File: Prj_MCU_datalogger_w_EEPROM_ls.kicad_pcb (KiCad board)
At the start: 2 copper layers, 57.1 x 36.8 mm, 29 parts, among them J1 Conn_01x04_Pin, J2 Conn_01x04_Pin, J3 Conn_01x09_Pin, J4 Conn_02x03_Odd_Even, U1 24LC1025, U2 24LC1025, U3 ATMEGA328P-AU, U4 DS1337S_, Y1 16 MHz, Y2 32.768 kHz

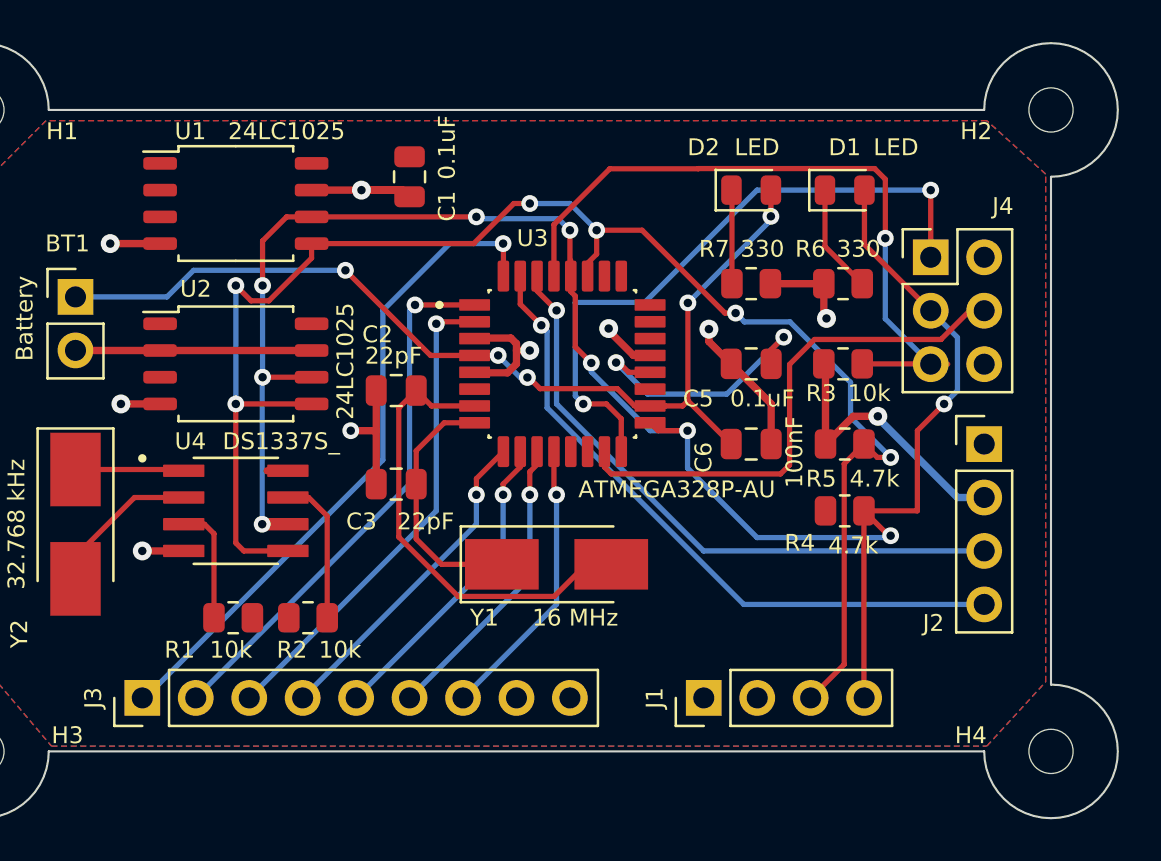
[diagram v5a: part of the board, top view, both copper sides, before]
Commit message: Refined routing.v3
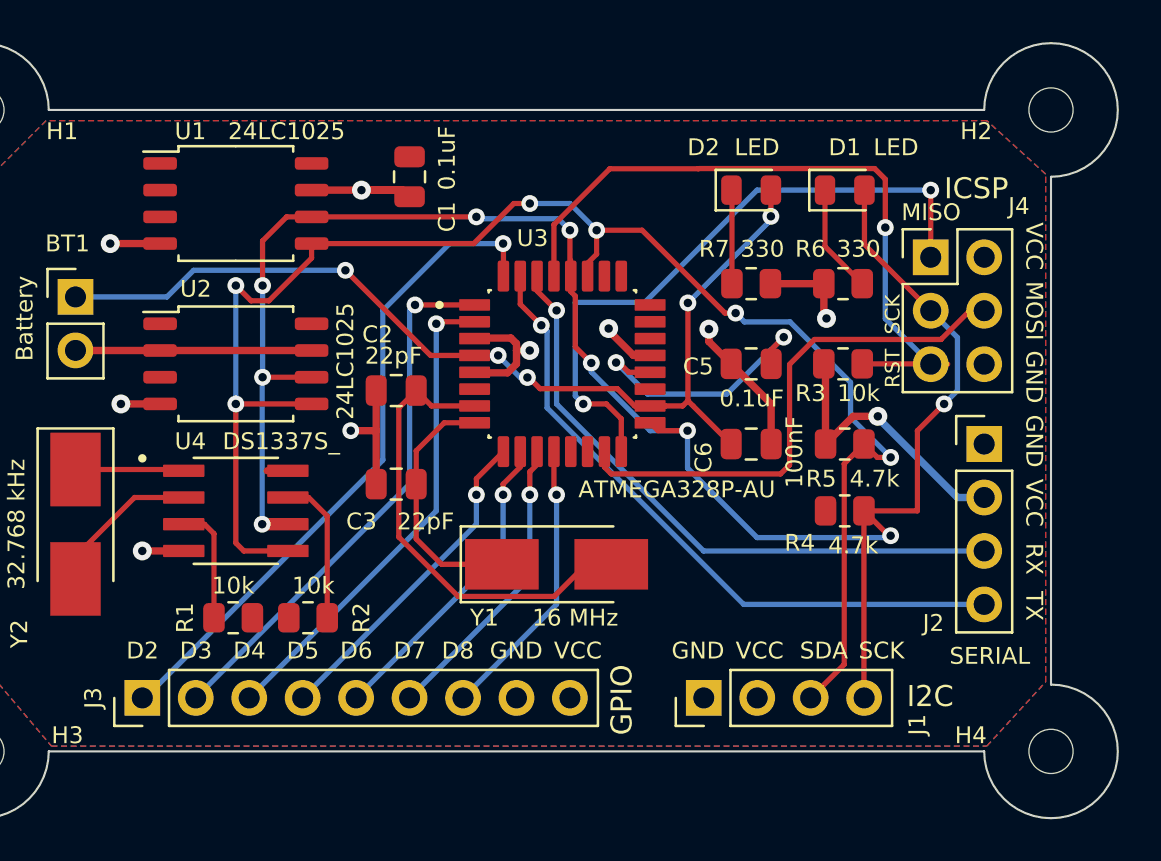
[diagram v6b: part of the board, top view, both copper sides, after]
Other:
- board text added: "D2"
- board text added: "D3"
- board text added: "D4"
- board text added: "D5"
- board text added: "D6"
- board text added: "D7"
- board text added: "D8"
- board text added: "GND"
- board text added: "GPIO"
- board text added: "I2C"
- board text added: "ICSP"
- board text added: "MISO"
- board text added: "MOSI"
- board text added: "RST"
- board text added: "RX"
- board text added: "SCK"
- board text added: "SDA"
- board text added: "SERIAL"
- board text added: "TX"
- board text added: "VCC"
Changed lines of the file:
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@@
     (property "ki_keywords" "connector")
     (attr through_hole)
-    (fp_text reference "J1" (at 0 -2.33 90) (layer "F.SilkS")
+    (fp_text reference "J1" (at -1.27 10.15 90) (layer "F.SilkS")
         (effects (font (size 0.8 0.8) (thickness 0.15)))
     )
@@
     (property "ki_keywords" "cap capacitor")
     (attr smd)
-    (fp_text reference "C5" (at -2.5165 1.651 180) (layer "F.SilkS")
-        (effects (font (size 0.8 0.8) (thickness 0.15)))
-    )
-    (fp_text value "0.1uF" (at 0.5315 1.651) (layer "F.SilkS")
+    (fp_text reference "C5" (at -2.5165 0.127 180) (layer "F.SilkS")
+        (effects (font (size 0.8 0.8) (thickness 0.15)))
+    )
+    (fp_text value "0.1uF" (at 0.0235 1.651) (layer "F.SilkS")
         (effects (font (size 0.8 0.8) (thickness 0.15)))
     )
@@
     (property "ki_keywords" "cap capacitor")
     (attr smd)
-    (fp_text reference "C1" (at 1.397 -1.778 90) (layer "F.SilkS")
-        (effects (font (size 0.8 0.8) (thickness 0.15)))
-    )
-    (fp_text value "0.1uF" (at -1.397 -1.778 90) (layer "F.SilkS")
+    (fp_text reference "C1" (at 1.905 -1.778 90) (layer "F.SilkS")
+        (effects (font (size 0.8 0.8) (thickness 0.15)))
+    )
+    (fp_text value "0.1uF" (at -0.889 -1.778 90) (layer "F.SilkS")
         (effects (font (size 0.8 0.8) (thickness 0.15)))
     )
@@
     (property "ki_keywords" "R res resistor")
     (attr smd)
-    (fp_text reference "R2" (at -0.762 1.524) (layer "F.SilkS")
-        (effects (font (size 0.8 0.8) (thickness 0.15)))
-    )
-    (fp_text value "10k" (at 1.524 1.524) (layer "F.SilkS")
+    (fp_text reference "R2" (at 2.54 0 90) (layer "F.SilkS")
+        (effects (font (size 0.8 0.8) (thickness 0.15)))
+    )
+    (fp_text value "10k" (at 0.254 -1.524) (layer "F.SilkS")
         (effects (font (size 0.8 0.8) (thickness 0.15)))
     )
@@
     (property "ki_keywords" "R res resistor")
     (attr smd)
-    (fp_text reference "R3" (at -1.0395 1.397) (layer "F.SilkS")
-        (effects (font (size 0.8 0.8) (thickness 0.15)))
-    )
-    (fp_text value "10k" (at 1.2465 1.397) (layer "F.SilkS")
+    (fp_text reference "R3" (at -1.5475 1.397) (layer "F.SilkS")
+        (effects (font (size 0.8 0.8) (thickness 0.15)))
+    )
+    (fp_text value "10k" (at 0.7385 1.397) (layer "F.SilkS")
         (effects (font (size 0.8 0.8) (thickness 0.15)))
     )
@@
     (property "ki_keywords" "connector")
     (attr through_hole)
-    (fp_text reference "J4" (at 3.429 -2.428) (layer "F.SilkS")
+    (fp_text reference "J4" (at 4.191 -2.428) (layer "F.SilkS")
         (effects (font (size 0.8 0.8) (thickness 0.15)))
     )
@@
     (property "ki_keywords" "R res resistor")
     (attr smd)
-    (fp_text reference "R1" (at 2.54 -1.524) (layer "F.SilkS")
-        (effects (font (size 0.8 0.8) (thickness 0.15)))
-    )
-    (fp_text value "10k" (at 0.1035 -1.524) (layer "F.SilkS")
+    (fp_text reference "R1" (at 2.286 0 90) (layer "F.SilkS")
+        (effects (font (size 0.8 0.8) (thickness 0.15)))
+    )
+    (fp_text value "10k" (at 0 1.524) (layer "F.SilkS")
         (effects (font (size 0.8 0.8) (thickness 0.15)))
     )
@@
   (gr_arc (start 271.78 154.305) (mid 274.025064 159.725064) (end 268.605 157.48)
     (stroke (width 0.1) (type default)) (layer "Edge.Cuts"))
+  (gr_text "GND" (at 270.51 138.43 270) (layer "F.SilkS")
+    (effects (font (size 0.8 0.8) (thickness 0.15)) (justify left bottom))
+  )
+  (gr_text "TX" (at 270.51 149.86 270) (layer "F.SilkS")
+    (effects (font (size 0.8 0.8) (thickness 0.15)) (justify left bottom))
+  )
+  (gr_text "D8" (at 242.824 153.162) (layer "F.SilkS")
+    (effects (font (size 0.8 0.8) (thickness 0.15)) (justify left bottom))
+  )
+  (gr_text "D2" (at 227.838 153.162) (layer "F.SilkS")
+    (effects (font (size 0.8 0.8) (thickness 0.15)) (justify left bottom))
+  )
+  (gr_text "D7" (at 240.538 153.162) (layer "F.SilkS")
+    (effects (font (size 0.8 0.8) (thickness 0.15)) (justify left bottom))
+  )
+  (gr_text "GND" (at 245.11 153.162) (layer "F.SilkS")
+    (effects (font (size 0.8 0.8) (thickness 0.15)) (justify left bottom))
+  )
+  (gr_text "SCK" (at 264.668 137.668 90) (layer "F.SilkS")
+    (effects (font (size 0.7 0.7) (thickness 0.15)) (justify left bottom))
+  )
+  (gr_text "D4" (at 232.918 153.162) (layer "F.SilkS")
+    (effects (font (size 0.8 0.8) (thickness 0.15)) (justify left bottom))
+  )
+  (gr_text "VCC" (at 270.51 132.334 270) (layer "F.SilkS")
+    (effects (font (size 0.8 0.8) (thickness 0.15)) (justify left bottom))
+  )
+  (gr_text "MISO" (at 264.668 132.334) (layer "F.SilkS")
+    (effects (font (size 0.8 0.8) (thickness 0.15)) (justify left bottom))
+  )
+  (gr_text "MOSI" (at 270.51 135.128 270) (layer "F.SilkS")
+    (effects (font (size 0.8 0.8) (thickness 0.15)) (justify left bottom))
+  )
+  (gr_text "VCC" (at 270.51 144.526 -90) (layer "F.SilkS")
+    (effects (font (size 0.8 0.8) (thickness 0.15)) (justify left bottom))
+  )
+  (gr_text "SERIAL" (at 266.954 153.416) (layer "F.SilkS")
+    (effects (font (size 0.8 0.8) (thickness 0.15)) (justify left bottom))
+  )
+  (gr_text "VCC" (at 256.794 153.162) (layer "F.SilkS")
+    (effects (font (size 0.8 0.8) (thickness 0.15)) (justify left bottom))
+  )
+  (gr_text "I2C" (at 264.922 155.448) (layer "F.SilkS")
+    (effects (font (size 1 1) (thickness 0.15)) (justify left bottom))
+  )
+  (gr_text "D5" (at 235.458 153.162) (layer "F.SilkS")
+    (effects (font (size 0.8 0.8) (thickness 0.15)) (justify left bottom))
+  )
+  (gr_text "ICSP" (at 266.7 131.318) (layer "F.SilkS")
+    (effects (font (size 1 1) (thickness 0.15)) (justify left bottom))
+  )
+  (gr_text "SDA" (at 259.842 153.162) (layer "F.SilkS")
+    (effects (font (size 0.8 0.8) (thickness 0.15)) (justify left bottom))
+  )
+  (gr_text "RST" (at 264.668 140.208 90) (layer "F.SilkS")
+    (effects (font (size 0.7 0.7) (thickness 0.15)) (justify left bottom))
+  )
+  (gr_text "GPIO" (at 251.968 156.718 90) (layer "F.SilkS")
+    (effects (font (size 1 1) (thickness 0.15)) (justify left bottom))
+  )
+  (gr_text "D3" (at 230.378 153.162) (layer "F.SilkS")
+    (effects (font (size 0.8 0.8) (thickness 0.15)) (justify left bottom))
+  )
+  (gr_text "VCC" (at 248.158 153.162) (layer "F.SilkS")
+    (effects (font (size 0.8 0.8) (thickness 0.15)) (justify left bottom))
+  )
+  (gr_text "GND" (at 253.746 153.162) (layer "F.SilkS")
+    (effects (font (size 0.8 0.8) (thickness 0.15)) (justify left bottom))
+  )
+  (gr_text "SCK" (at 262.636 153.162) (layer "F.SilkS")
+    (effects (font (size 0.8 0.8) (thickness 0.15)) (justify left bottom))
+  )
+  (gr_text "D6" (at 237.998 153.162) (layer "F.SilkS")
+    (effects (font (size 0.8 0.8) (thickness 0.15)) (justify left bottom))
+  )
+  (gr_text "RX" (at 270.51 147.574 270) (layer "F.SilkS")
+    (effects (font (size 0.8 0.8) (thickness 0.15)) (justify left bottom))
+  )
+  (gr_text "GND" (at 270.51 141.478 -90) (layer "F.SilkS")
+    (effects (font (size 0.8 0.8) (thickness 0.15)) (justify left bottom))
+  )
   (segment (start 238.252 134.62) (end 242.297 138.665) (width 0.25) (layer "F.Cu") (net 1))
   (segment (start 251.175001 140.245) (end 251.995001 141.065) (width 0.25) (layer "F.Cu") (net 1))
@@
   (segment (start 267.916701 136.54) (end 266.551701 137.905) (width 0.25) (layer "F.Cu") (net 21))
   (segment (start 250.56 143.969999) (end 250.56 143.235) (width 0.25) (layer "F.Cu") (net 21))
+  (segment (start 263.906 130.289912) (end 263.401088 129.785) (width 0.25) (layer "F.Cu") (net 22))
+  (segment (start 248.16 132.449695) (end 248.16 134.895) (width 0.25) (layer "F.Cu") (net 22))
   (segment (start 266.872588 139.08) (end 266.065 139.08) (width 0.25) (layer "F.Cu") (net 22))
+  (segment (start 255.025 129.785) (end 255.016 129.794) (width 0.25) (layer "F.Cu") (net 22))
   (segment (start 266.05 139.065) (end 266.065 139.08) (width 0.25) (layer "F.Cu") (net 22))
-  (segment (start 263.401088 129.785) (end 263.906 130.289912) (width 0.25) (layer "F.Cu") (net 22))
+  (segment (start 263.906 132.588) (end 263.906 130.289912) (width 0.25) (layer "F.Cu") (net 22))
   (segment (start 262.81 139.065) (end 266.05 139.065) (width 0.25) (layer "F.Cu") (net 22))
-  (segment (start 255.025 129.785) (end 263.401088 129.785) (width 0.25) (layer "F.Cu") (net 22))
-  (segment (start 248.16 132.449695) (end 250.815695 129.794) (width 0.25) (layer "F.Cu") (net 22))
-  (segment (start 248.16 134.895) (end 248.16 132.449695) (width 0.25) (layer "F.Cu") (net 22))
-  (segment (start 255.016 129.794) (end 255.025 129.785) (width 0.25) (layer "F.Cu") (net 22))
-  (segment (start 250.815695 129.794) (end 255.016 129.794) (width 0.25) (layer "F.Cu") (net 22))
-  (segment (start 263.906 130.289912) (end 263.906 133.096) (width 0.25) (layer "F.Cu") (net 22))
-  (via (at 263.906 133.096) (size 0.8) (drill 0.4) (layers "F.Cu" "B.Cu") (net 22))
+  (segment (start 263.401088 129.785) (end 255.025 129.785) (width 0.25) (layer "F.Cu") (net 22))
+  (segment (start 255.016 129.794) (end 250.815695 129.794) (width 0.25) (layer "F.Cu") (net 22))
+  (segment (start 250.815695 129.794) (end 248.16 132.449695) (width 0.25) (layer "F.Cu") (net 22))
+  (via (at 263.906 132.588) (size 0.8) (drill 0.4) (layers "F.Cu" "B.Cu") (net 22))
+  (segment (start 263.906 132.588) (end 263.906 136.921) (width 0.25) (layer "B.Cu") (net 22))
   (segment (start 263.906 136.921) (end 266.065 139.08) (width 0.25) (layer "B.Cu") (net 22))
-  (segment (start 263.906 133.096) (end 263.906 136.921) (width 0.25) (layer "B.Cu") (net 22))
   (segment (start 231.554999 146.685) (end 230.57 146.685) (width 0.25) (layer "F.Cu") (net 23))
   (segment (start 232.0055 147.135501) (end 231.554999 146.685) (width 0.25) (layer "F.Cu") (net 23))

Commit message: Refined routing.v4
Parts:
- moved C2 0.38 mm to (240.7, 140.7)
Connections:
- BT1 pad 1: Net-(BT1-+) -> /Vcc
- C6 pad 1: Net-(BT1-+) -> /Vcc
- D2 pad 2: Net-(BT1-+) -> /Vcc
- U3 pad 18: Net-(BT1-+) -> /Vcc
- U3 pad 4: Net-(BT1-+) -> /Vcc
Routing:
- net Net-(BT1-+): track 47.7 -> 0.00 mm, vias 5 -> 0
- net /Vcc: track 15.3 -> 50.3 mm, vias 1 -> 5

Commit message: Fixed issues
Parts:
- added REF**: KiCad-Logo2_5mm_SilkScreen, Symbol:KiCad-Logo2_5mm_SilkScreen, B.Cu at (258.5, 134.2)
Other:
- board text added: "- 2 Mbit EEPROM - RTC - I2C, SPI, GPIOs"
- board text added: "202312-LS"
- board text added: "Data Logger with ATMEGA328P"
- board text added: "v.01"
